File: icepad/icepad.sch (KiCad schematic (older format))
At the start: 46 parts, among them U1 STM32F042F6Px

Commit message: Added PCB footprint and associated schematic to footprints
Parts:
- C1, C2, C3, C4, C5, C6, C7: renamed from C?; footprint (none) -> Capacitor_SMD:C_0805_2012Metric_Pad1.15x1.40mm_HandSolder
- D1, D10, D11, D12, D13, D14, D15, D16, D2, D3, D4, D5, D6, D7, D8, D9: renamed from D?; footprint (none) -> Diode_THT:D_DO-35_SOD27_P7.62mm_Horizontal
- L1: renamed from L?; footprint (none) -> Inductor_SMD:L_0805_2012Metric_Pad1.15x1.40mm_HandSolder
- MX1, MX10, MX11, MX12, MX13, MX14, MX15, MX16, MX2, MX3, MX4, MX5, MX6, MX7, MX8, MX9: renamed from MX?; footprint (none) -> MX_Only:MXOnly-1U-Hotswap
- R1, R2: renamed from R?; footprint (none) -> Resistor_SMD:R_0805_2012Metric_Pad1.15x1.40mm_HandSolder
- U3: renamed from U?; footprint (none) -> IES0105S03:IES0105S03
- USB1: renamed from USB?; footprint (none) -> Type-C:Wurth-632723300011-HandSoldering
- gave numbers to parts that had none: 1
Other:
- note added: "Diodes are 1n4148 compatible THT"
- note added: "Switch Array"

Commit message: set up key grid on PCB layout
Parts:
- removed U1: STM32F042F6Px, Package_SO:TSSOP-20_4.4x6.5mm_P0.65mm, symbol MCU_ST_STM32F0:STM32F042F6Px
- added C10, C9: 4.7uF, Capacitor_SMD:C_0805_2012Metric_Pad1.15x1.40mm_HandSolder, symbol Device:C_Small
- added C8: 1uF, Capacitor_SMD:C_0805_2012Metric_Pad1.15x1.40mm_HandSolder, symbol Device:C_Small
- added R3: 5k1, Resistor_SMD:R_0805_2012Metric_Pad1.15x1.40mm_HandSolder, symbol Device:R_Small
- added U1: STM32F042K6Tx, Package_QFP:LQFP-32_7x7mm_P0.8mm, symbol MCU_ST_STM32F0:STM32F042K6Tx
- C2: value 100nF -> 10nF
- C4: value 4.7uF -> 100nF
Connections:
- net labels removed: USB_DM, USB_DP
- wire segments 219 -> 237
- no-connect marks 14 -> 10
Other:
- note added: "MCU VDD"
- note added: "MCU VDDA"
- note added: "MCU VDDIO2"

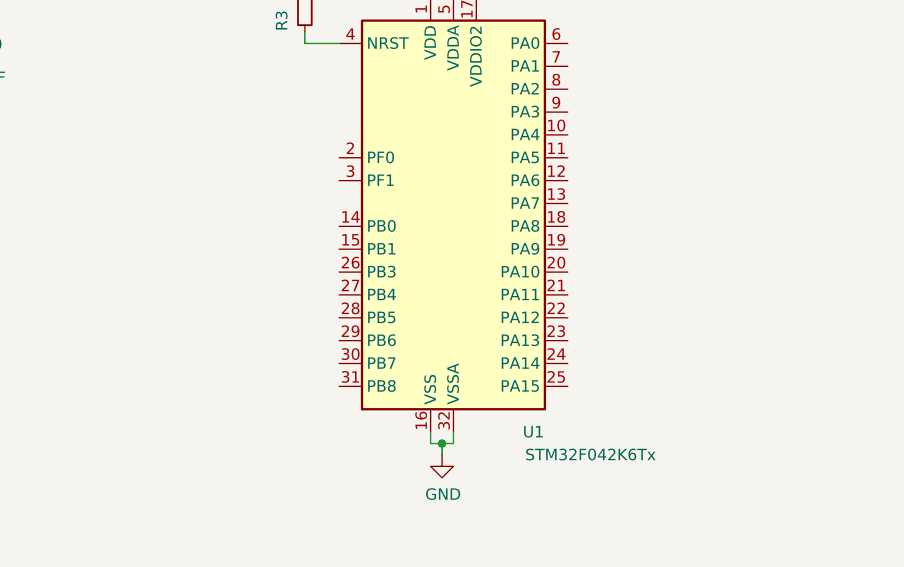
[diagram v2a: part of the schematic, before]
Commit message: completed routing without led
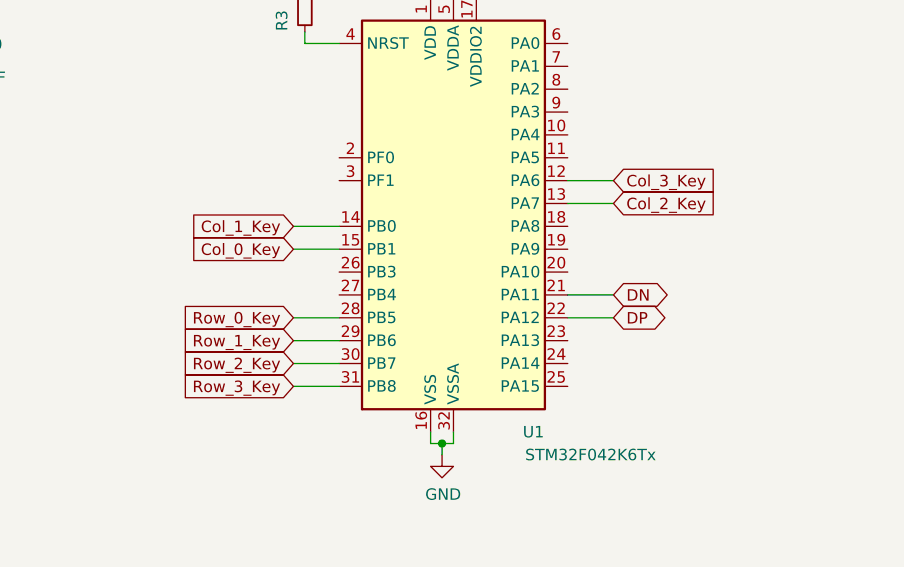
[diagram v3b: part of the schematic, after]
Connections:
- wire segments 237 -> 247
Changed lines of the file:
@@
 Wire Wire Line
 	3250 4300 3250 4350
+Text GLabel 4600 5700 2    50   BiDi ~ 0
+DN
+Text GLabel 4600 5800 2    50   BiDi ~ 0
+DP
+Wire Wire Line
+	4600 5700 4400 5700
+Wire Wire Line
+	4400 5800 4600 5800
+Text GLabel 3200 6100 0    50   Input ~ 0
+Row_3_Key
+Text GLabel 3200 6000 0    50   Input ~ 0
+Row_2_Key
+Text GLabel 3200 5900 0    50   Input ~ 0
+Row_1_Key
+Text GLabel 3200 5800 0    50   Input ~ 0
+Row_0_Key
+Wire Wire Line
+	3200 5800 3400 5800
+Wire Wire Line
+	3200 5900 3400 5900
+Wire Wire Line
+	3200 6000 3400 6000
+Wire Wire Line
+	3200 6100 3400 6100
+Text GLabel 3200 5500 0    50   Input ~ 0
+Col_0_Key
+Text GLabel 4600 5300 2    50   Input ~ 0
+Col_2_Key
+Text GLabel 4600 5200 2    50   Input ~ 0
+Col_3_Key
+Text GLabel 3200 5400 0    50   Input ~ 0
+Col_1_Key
+Wire Wire Line
+	3200 5400 3400 5400
+Wire Wire Line
+	3400 5500 3200 5500
+Wire Wire Line
+	4600 5300 4400 5300
+Wire Wire Line
+	4600 5200 4400 5200
 $EndSCHEMATC

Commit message: added jlcpcb stock and new pcb design
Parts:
- removed C10, C5: 4.7uF, Capacitor_SMD:C_0805_2012Metric_Pad1.15x1.40mm_HandSolder, symbol Device:C_Small
- removed D1, D10, D11, D12, D13, D14, D15, D16, D2, D3, D4, D5, D6, D7, D8, D9: D_Small, Diode_THT:D_DO-35_SOD27_P7.62mm_Horizontal, symbol Device:D_Small
- removed U2: TPD2EUSB30A, Package_TO_SOT_SMD:Texas_DRT-3, symbol Power_Protection:TPD2EUSB30A
- removed U3: IES0105S03, IES0105S03:IES0105S03, symbol IES0105S03:IES0105S03
- added C8: 4.7uF, Capacitor_SMD:C_0805_2012Metric_Pad1.15x1.40mm_HandSolder, symbol Device:C_Small
- added D1, D10, D11, D12, D13, D14, D15, D16, D2, D3, D4, D5, D6, D7, D8, D9: 1N4148WS, Diode_SMD:D_SOD-323, symbol Diode:1N4148WS
- added J1: Conn_01x04, Connector_PinHeader_2.54mm:PinHeader_1x04_P2.54mm_Horizontal, symbol Connector_Generic:Conn_01x04
- added R4: 453k, Resistor_SMD:R_0805_2012Metric, symbol Device:R_Small
- added R5: 100k, Resistor_SMD:R_0805_2012Metric, symbol Device:R_Small
- added U2: USBLC6-2SC6, Package_TO_SOT_SMD:SOT-23-6, symbol Power_Protection:USBLC6-2SC6
- added U3: TLV62568DRL, Package_TO_SOT_SMD:SOT-563, symbol Regulator_Switching:TLV62568DRL
- C1, C3, C4: LCSC (none) -> C49678
- C2: LCSC (none) -> C1710
- C5: renamed from C8; LCSC (none) -> C28323
- C6: LCSC (none) -> C1779
- C7: value 10uF -> 4.7uF; LCSC (none) -> C1779
- C9: value 4.7uF -> 10uF; LCSC (none) -> C15850
- L1: value 6.8uH -> 2.2uH; footprint Inductor_SMD:L_0805_2012Metric_Pad1.15x1.40mm_HandSolder -> Inductor_SMD:L_0805_2012Metric; LCSC (none) -> C1043
- MX1, MX10, MX11, MX12, MX13, MX14, MX15, MX16, MX2, MX3, MX4, MX5, MX6, MX7, MX8, MX9: footprint MX_Only:MXOnly-1U-Hotswap -> MX_Only:MXOnly-1U; symbol MX_Alps_Hybrid:MX-LED -> icepad-rescue:MX-LED-MX_Alps_Hybrid
- R1, R2, R3: LCSC (none) -> C27834
- U1: LCSC (none) -> C69216
- USB1: symbol Type-C:Wurth-632723300011 -> icepad-rescue:Wurth-632723300011-Type-C
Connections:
- net labels added: SWCLK, SWDIO
- wire segments 247 -> 269
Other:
- note added: "Programming Connector"
- note removed: "Diodes are 1n4148 compatible THT"

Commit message: complete new pcba design
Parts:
- removed R2: 5k1, Resistor_SMD:R_0805_2012Metric_Pad1.15x1.40mm_HandSolder, symbol Device:R_Small
- removed USB1: Wurth-632723300011, Type-C:Wurth-632723300011-HandSoldering, symbol icepad-rescue:Wurth-632723300011-Type-C
- added C10: 100nF, Capacitor_SMD:C_0805_2012Metric, symbol Device:C_Small
- added J2: USB_B_Mini, digikey-footprints:USB_Mini_B_Female_548190519, symbol Connector:USB_B_Mini
- C1, C2, C3, C4, C5, C6, C7, C8, C9: footprint Capacitor_SMD:C_0805_2012Metric_Pad1.15x1.40mm_HandSolder -> Capacitor_SMD:C_0805_2012Metric
- R1: value 5k1 -> 330; footprint Resistor_SMD:R_0805_2012Metric_Pad1.15x1.40mm_HandSolder -> Resistor_SMD:R_0805_2012Metric; LCSC C27834 -> C17630
- R3: footprint Resistor_SMD:R_0805_2012Metric_Pad1.15x1.40mm_HandSolder -> Resistor_SMD:R_0805_2012Metric
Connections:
- net Col_0_Key: no longer U1.15 (PB1)
- net Col_1_Key: no longer U1.14 (PB0)
- net Col_2_Key: no longer U1.13 (PA7)
- net Col_3_Key: no longer U1.12 (PA6)
- net DN: no longer U2.4 (IO2)
- net DP: no longer U2.6 (IO1)
- net GND: now also R1.2, C10.1, J2.5 (GND); no longer R1.1
- net Row_0_Key: no longer U1.28 (PB5)
- net Row_1_Key: no longer U1.29 (PB6)
- net Row_2_Key: no longer U1.30 (PB7)
- net Row_3_Key: no longer U1.31 (PB8)
- net VBUS: now also J2.1 (VBUS)
- new net: C10.2, J2.6 (Shield), R1.1
- new net DN_pre: J2.2 (D-), U2.4 (IO2)
- new net DP_pre: J2.3 (D+), U2.6 (IO1)
- no-connect marks 10 -> 1
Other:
- note added: "USB Socket"
- note removed: "USB C Socket"
- moved on the sheet: J1

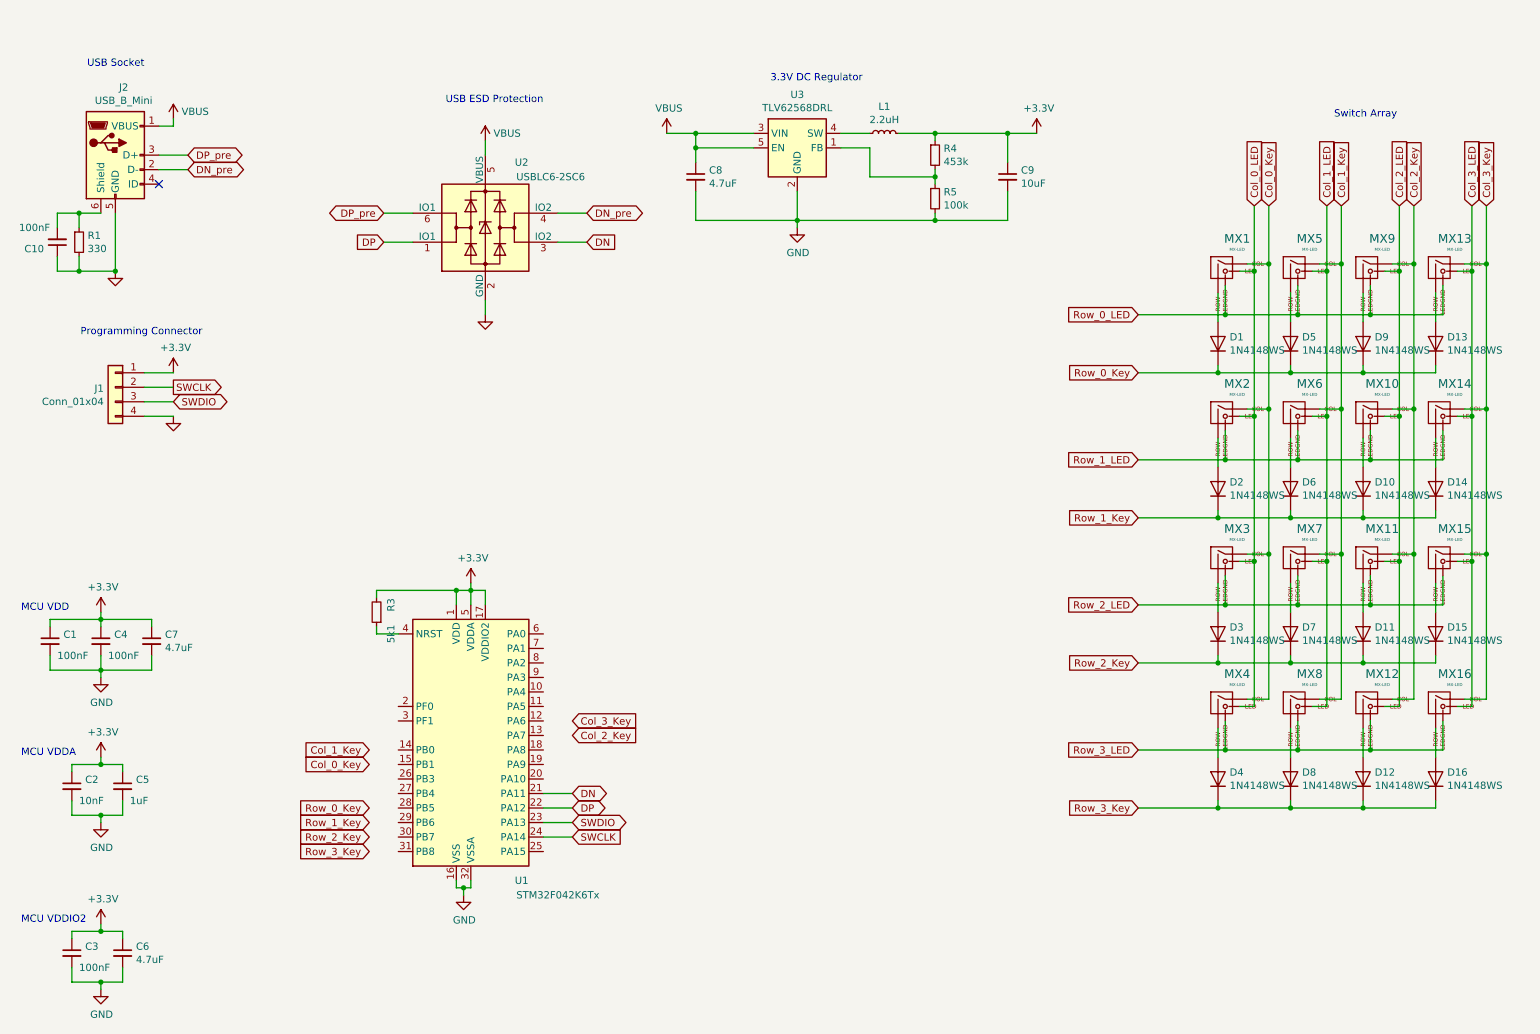
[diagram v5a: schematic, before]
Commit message: Completed routing, added LED resistors
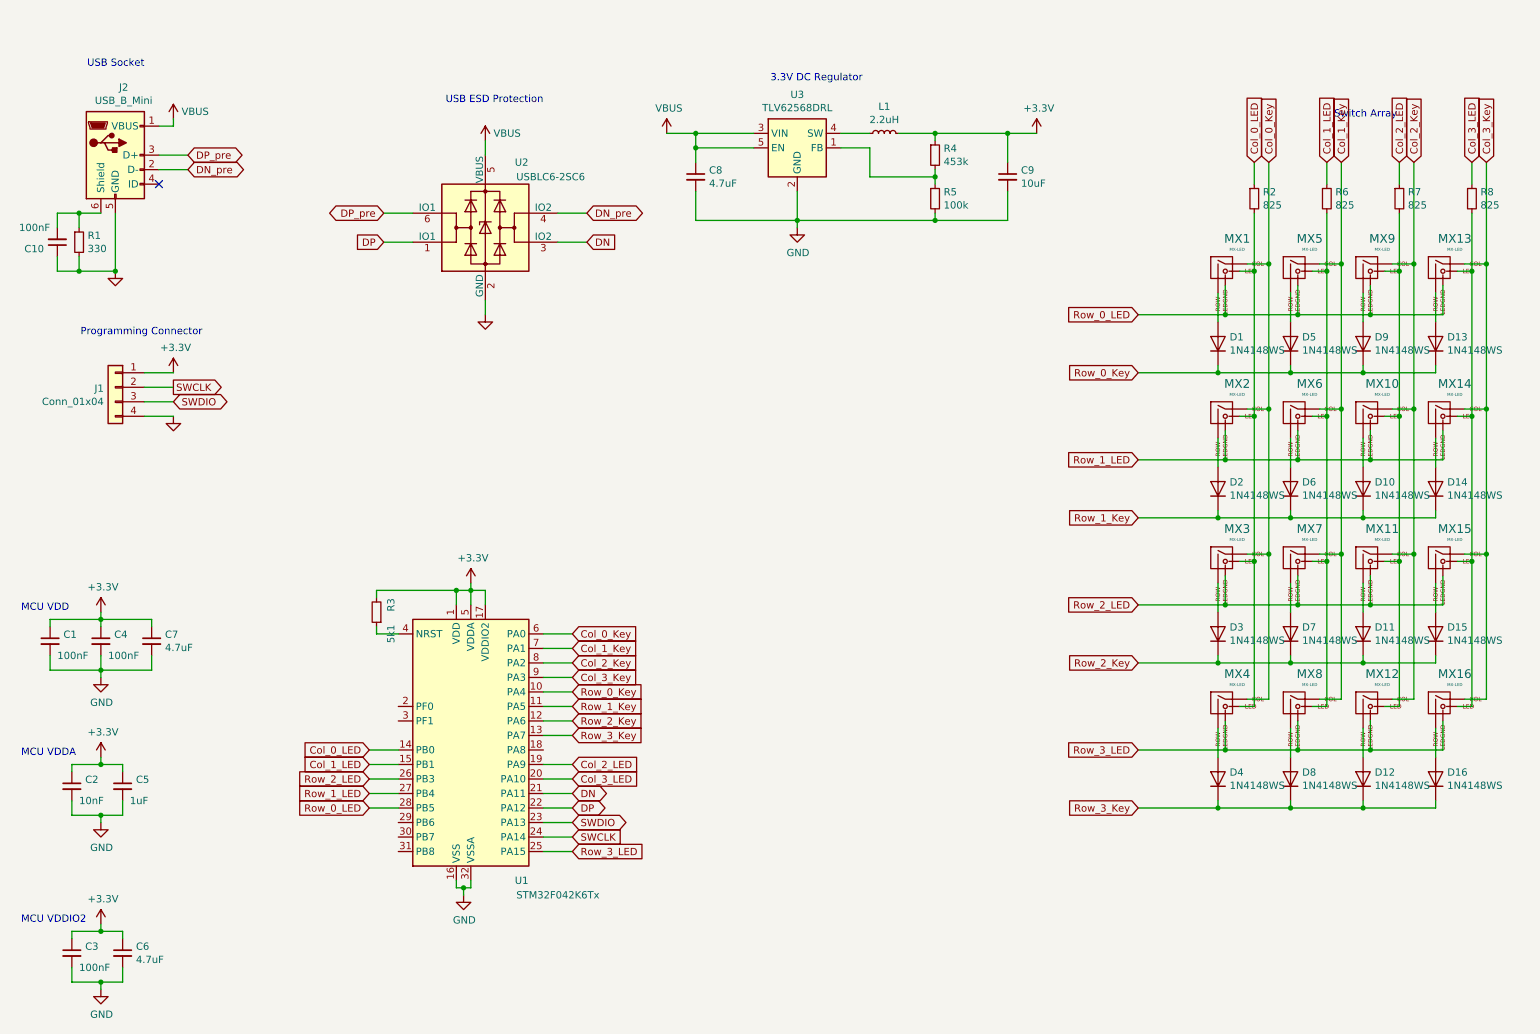
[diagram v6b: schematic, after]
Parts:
- added R2, R6, R7, R8: 825, Resistor_SMD:R_0805_2012Metric, symbol Device:R_Small
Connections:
- net Col_0_Key: now also U1.6 (PA0)
- net Col_0_LED: now also U1.14 (PB0), R2.1; no longer MX1.3 (LED), MX2.3 (LED), MX3.3 (LED), MX4.3 (LED)
- net Col_1_Key: now also U1.7 (PA1)
- net Col_1_LED: now also U1.15 (PB1), R6.1; no longer MX5.3 (LED), MX6.3 (LED), MX7.3 (LED), MX8.3 (LED)
- net Col_2_Key: now also U1.8 (PA2)
- net Col_2_LED: now also U1.19 (PA9), R7.1; no longer MX10.3 (LED), MX11.3 (LED), MX12.3 (LED), MX9.3 (LED)
- net Col_3_Key: now also U1.9 (PA3)
- net Col_3_LED: now also U1.20 (PA10), R8.1; no longer MX13.3 (LED), MX14.3 (LED), MX15.3 (LED), MX16.3 (LED)
- net Row_0_Key: now also U1.10 (PA4)
- net Row_0_LED: now also U1.28 (PB5)
- net Row_1_Key: now also U1.11 (PA5)
- net Row_1_LED: now also U1.27 (PB4)
- net Row_2_Key: now also U1.12 (PA6)
- net Row_2_LED: now also U1.26 (PB3)
- net Row_3_Key: now also U1.13 (PA7)
- net Row_3_LED: now also U1.25 (PA15)
- new net: MX1.3 (LED), MX2.3 (LED), MX3.3 (LED), MX4.3 (LED), R2.2
- new net: MX5.3 (LED), MX6.3 (LED), MX7.3 (LED), MX8.3 (LED), R6.2
- new net: MX10.3 (LED), MX11.3 (LED), MX12.3 (LED), MX9.3 (LED), R7.2
- new net: MX13.3 (LED), MX14.3 (LED), MX15.3 (LED), MX16.3 (LED), R8.2
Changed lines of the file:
@@
 $EndComp
-Wire Wire Line
-	9400 1650 9400 2050
 Wire Wire Line
 	9250 2050 9400 2050
@@
 	9750 2050 9900 2050
 Wire Wire Line
-	9900 2050 9900 1650
-Wire Wire Line
 	10250 2050 10400 2050
 Wire Wire Line
 	10750 2050 10900 2050
 Wire Wire Line
-	10900 2050 10900 1650
-Wire Wire Line
 	9250 3050 9400 3050
 Wire Wire Line
@@
 	9250 4050 9400 4050
 Wire Wire Line
-	9300 1650 9300 2100
-Wire Wire Line
 	9200 4100 9300 4100
 Wire Wire Line
@@
 Wire Wire Line
 	9200 2100 9300 2100
-Wire Wire Line
-	9800 1650 9800 2100
-Wire Wire Line
-	10300 1650 10300 2100
-Wire Wire Line
-	10800 1650 10800 2100
 Wire Wire Line
 	9700 4100 9800 4100
@@
 Text GLabel 8500 4400 0    50   Input ~ 0
 Row_2_LED
-Text GLabel 9400 1650 1    50   Input ~ 0
+Text GLabel 9400 1350 1    50   Input ~ 0
 Col_0_Key
-Text GLabel 9300 1650 1    50   Input ~ 0
+Text GLabel 9300 1350 1    50   Input ~ 0
 Col_0_LED
-Text GLabel 9800 1650 1    50   Input ~ 0
+Text GLabel 9800 1350 1    50   Input ~ 0
 Col_1_LED
-Text GLabel 9900 1650 1    50   Input ~ 0
+Text GLabel 9900 1350 1    50   Input ~ 0
 Col_1_Key
-Text GLabel 10300 1650 1    50   Input ~ 0
+Text GLabel 10300 1350 1    50   Input ~ 0
 Col_2_LED
-Text GLabel 10400 1650 1    50   Input ~ 0
+Text GLabel 10400 1350 1    50   Input ~ 0
 Col_2_Key
-Text GLabel 10800 1650 1    50   Input ~ 0
+Text GLabel 10800 1350 1    50   Input ~ 0
 Col_3_LED
-Text GLabel 10900 1650 1    50   Input ~ 0
+Text GLabel 10900 1350 1    50   Input ~ 0
 Col_3_Key
 Text GLabel 8500 5400 0    50   Input ~ 0
@@
 Wire Wire Line
 	9300 2100 9300 3100
-Connection ~ 9300 2100
 Wire Wire Line
 	9400 2050 9400 3050
@@
 Wire Wire Line
 	9800 2100 9800 3100
-Connection ~ 9800 2100
 Wire Wire Line
 	9900 2050 9900 3050
@@
 Wire Wire Line
 	10300 2100 10300 3100
-Connection ~ 10300 2100
-Wire Wire Line
-	10400 1650 10400 2050
 Connection ~ 10400 2050
 Wire Wire Line
 	10400 2050 10400 3050
-Wire Wire Line
-	10800 2100 10800 3100
-Connection ~ 10800 2100
 Wire Wire Line
 	10900 2050 10900 3050
@@
 Wire Wire Line
 	4400 5800 4600 5800
-Text GLabel 3200 6100 0    50   Input ~ 0
+Text GLabel 4600 5300 2    50   Input ~ 0
 Row_3_Key
-Text GLabel 3200 6000 0    50   Input ~ 0
+Text GLabel 4600 5200 2    50   Input ~ 0
 Row_2_Key
-Text GLabel 3200 5900 0    50   Input ~ 0
+Text GLabel 4600 5100 2    50   Input ~ 0
 Row_1_Key
-Text GLabel 3200 5800 0    50   Input ~ 0
+Text GLabel 4600 5000 2    50   Input ~ 0
 Row_0_Key
-Text GLabel 3200 5500 0    50   Input ~ 0
+Text GLabel 4600 4600 2    50   Input ~ 0
 Col_0_Key
-Text GLabel 4600 5300 2    50   Input ~ 0
+Text GLabel 4600 4800 2    50   Input ~ 0
 Col_2_Key
-Text GLabel 4600 5200 2    50   Input ~ 0
+Text GLabel 4600 4900 2    50   Input ~ 0
 Col_3_Key
-Text GLabel 3200 5400 0    50   Input ~ 0
+Text GLabel 4600 4700 2    50   Input ~ 0
 Col_1_Key
 Wire Wire Line
@@
 Wire Wire Line
 	4500 1900 4700 1900
+Wire Wire Line
+	3200 5800 3400 5800
+Wire Wire Line
+	3200 5700 3400 5700
+Wire Wire Line
+	3200 5600 3400 5600
+Wire Wire Line
+	4400 6100 4600 6100
+Text GLabel 4600 6100 2    50   Input ~ 0
+Row_3_LED
+Text GLabel 3200 5600 0    50   Input ~ 0
+Row_2_LED
+Text GLabel 3200 5700 0    50   Input ~ 0
+Row_1_LED
+Text GLabel 3200 5800 0    50   Input ~ 0
+Row_0_LED
+Wire Wire Line
+	4600 4900 4400 4900
+Wire Wire Line
+	4600 4800 4400 4800
+Wire Wire Line
+	4600 4700 4400 4700
+Wire Wire Line
+	4600 4600 4400 4600
+Wire Wire Line
+	4600 5000 4400 5000
+Wire Wire Line
+	4400 5100 4600 5100
+Wire Wire Line
+	4600 5200 4400 5200
+Wire Wire Line
+	4400 5300 4600 5300
+Text GLabel 3200 5400 0    50   Input ~ 0
+Col_0_LED
+Text GLabel 3200 5500 0    50   Input ~ 0
+Col_1_LED
+Text GLabel 4600 5500 2    50   Input ~ 0
+Col_2_LED
+Text GLabel 4600 5600 2    50   Input ~ 0
+Col_3_LED
+Wire Wire Line
+	3200 5400 3400 5400
+Wire Wire Line
+	3400 5500 3200 5500
+Wire Wire Line
+	4600 5500 4400 5500
+Wire Wire Line
+	4600 5600 4400 5600
+Wire Wire Line
+	9400 1350 9400 2050
+Wire Wire Line
+	9900 1350 9900 2050
+Wire Wire Line
+	10400 1350 10400 2050
+Wire Wire Line
+	10900 1350 10900 2050
+$Comp
+L Device:R_Small R2
+U 1 1 5ECA9B18
+P 9300 1600
+F 0 "R2" H 9359 1646 50  0000 L CNN
+F 1 "825" H 9359 1555 50  0000 L CNN
+F 2 "Resistor_SMD:R_0805_2012Metric" H 9300 1600 50  0001 C CNN
+F 3 "~" H 9300 1600 50  0001 C CNN
+F 4 "C17839" H 9300 1600 50  0001 C CNN "LCSC"
+	1    9300 1600
+	1    0    0    -1
+$EndComp
+$Comp
+L Device:R_Small R6
+U 1 1 5ECAA5AE
+P 9800 1600
+F 0 "R6" H 9859 1646 50  0000 L CNN
+F 1 "825" H 9859 1555 50  0000 L CNN
+F 2 "Resistor_SMD:R_0805_2012Metric" H 9800 1600 50  0001 C CNN
+F 3 "~" H 9800 1600 50  0001 C CNN
+F 4 "C17839" H 9800 1600 50  0001 C CNN "LCSC"
+	1    9800 1600
+	1    0    0    -1
+$EndComp
+$Comp
+L Device:R_Small R7
+U 1 1 5ECAAB8D
+P 10300 1600
+F 0 "R7" H 10359 1646 50  0000 L CNN
+F 1 "825" H 10359 1555 50  0000 L CNN
+F 2 "Resistor_SMD:R_0805_2012Metric" H 10300 1600 50  0001 C CNN
+F 3 "~" H 10300 1600 50  0001 C CNN
+F 4 "C17839" H 10300 1600 50  0001 C CNN "LCSC"
+	1    10300 1600
+	1    0    0    -1
+$EndComp
+$Comp
+L Device:R_Small R8
+U 1 1 5ECAACAE
+P 10800 1600
+F 0 "R8" H 10859 1646 50  0000 L CNN
+F 1 "825" H 10859 1555 50  0000 L CNN
+F 2 "Resistor_SMD:R_0805_2012Metric" H 10800 1600 50  0001 C CNN
+F 3 "~" H 10800 1600 50  0001 C CNN
+F 4 "C17839" H 10800 1600 50  0001 C CNN "LCSC"
+	1    10800 1600
+	1    0    0    -1
+$EndComp
+Wire Wire Line
+	9300 1700 9300 2100
+Connection ~ 9300 2100
+Wire Wire Line
+	9300 1500 9300 1350
+Wire Wire Line
+	9800 1350 9800 1500
+Wire Wire Line
+	9800 1700 9800 2100
+Connection ~ 9800 2100
+Wire Wire Line
+	10300 1350 10300 1500
+Wire Wire Line
+	10300 1700 10300 2100
+Connection ~ 10300 2100
+Wire Wire Line
+	10800 1350 10800 1500
+Wire Wire Line
+	10800 1700 10800 2100
+Connection ~ 10800 2100
+Wire Wire Line
+	10800 2100 10800 3100
 $EndSCHEMATC
